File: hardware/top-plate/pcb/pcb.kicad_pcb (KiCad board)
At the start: 2 copper layers, 16 x 20 mm, 78 parts, among them SW1 MT-0-102-A101-M200-RS+PJ, U1 RP2040-ZERO

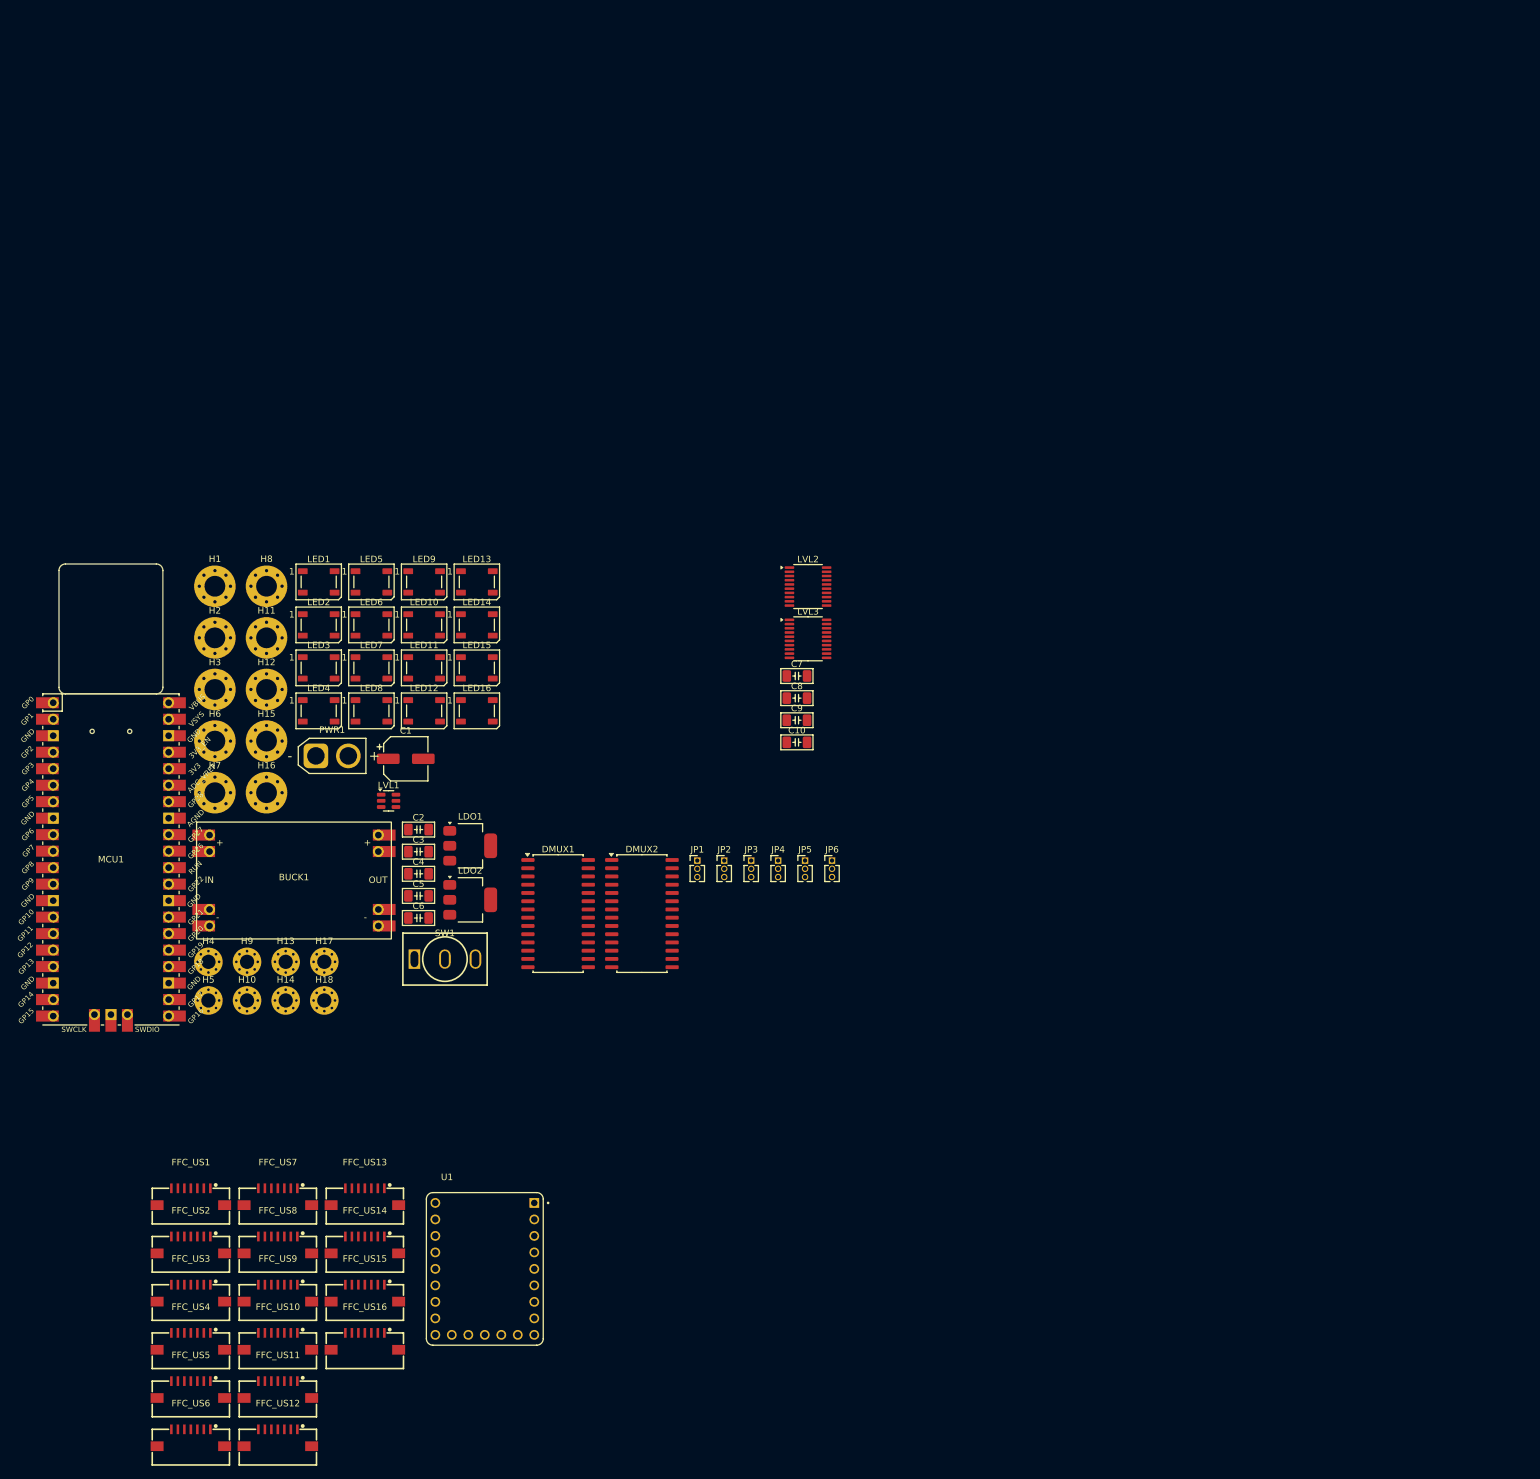
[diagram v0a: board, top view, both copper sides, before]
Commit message: some top plate changes
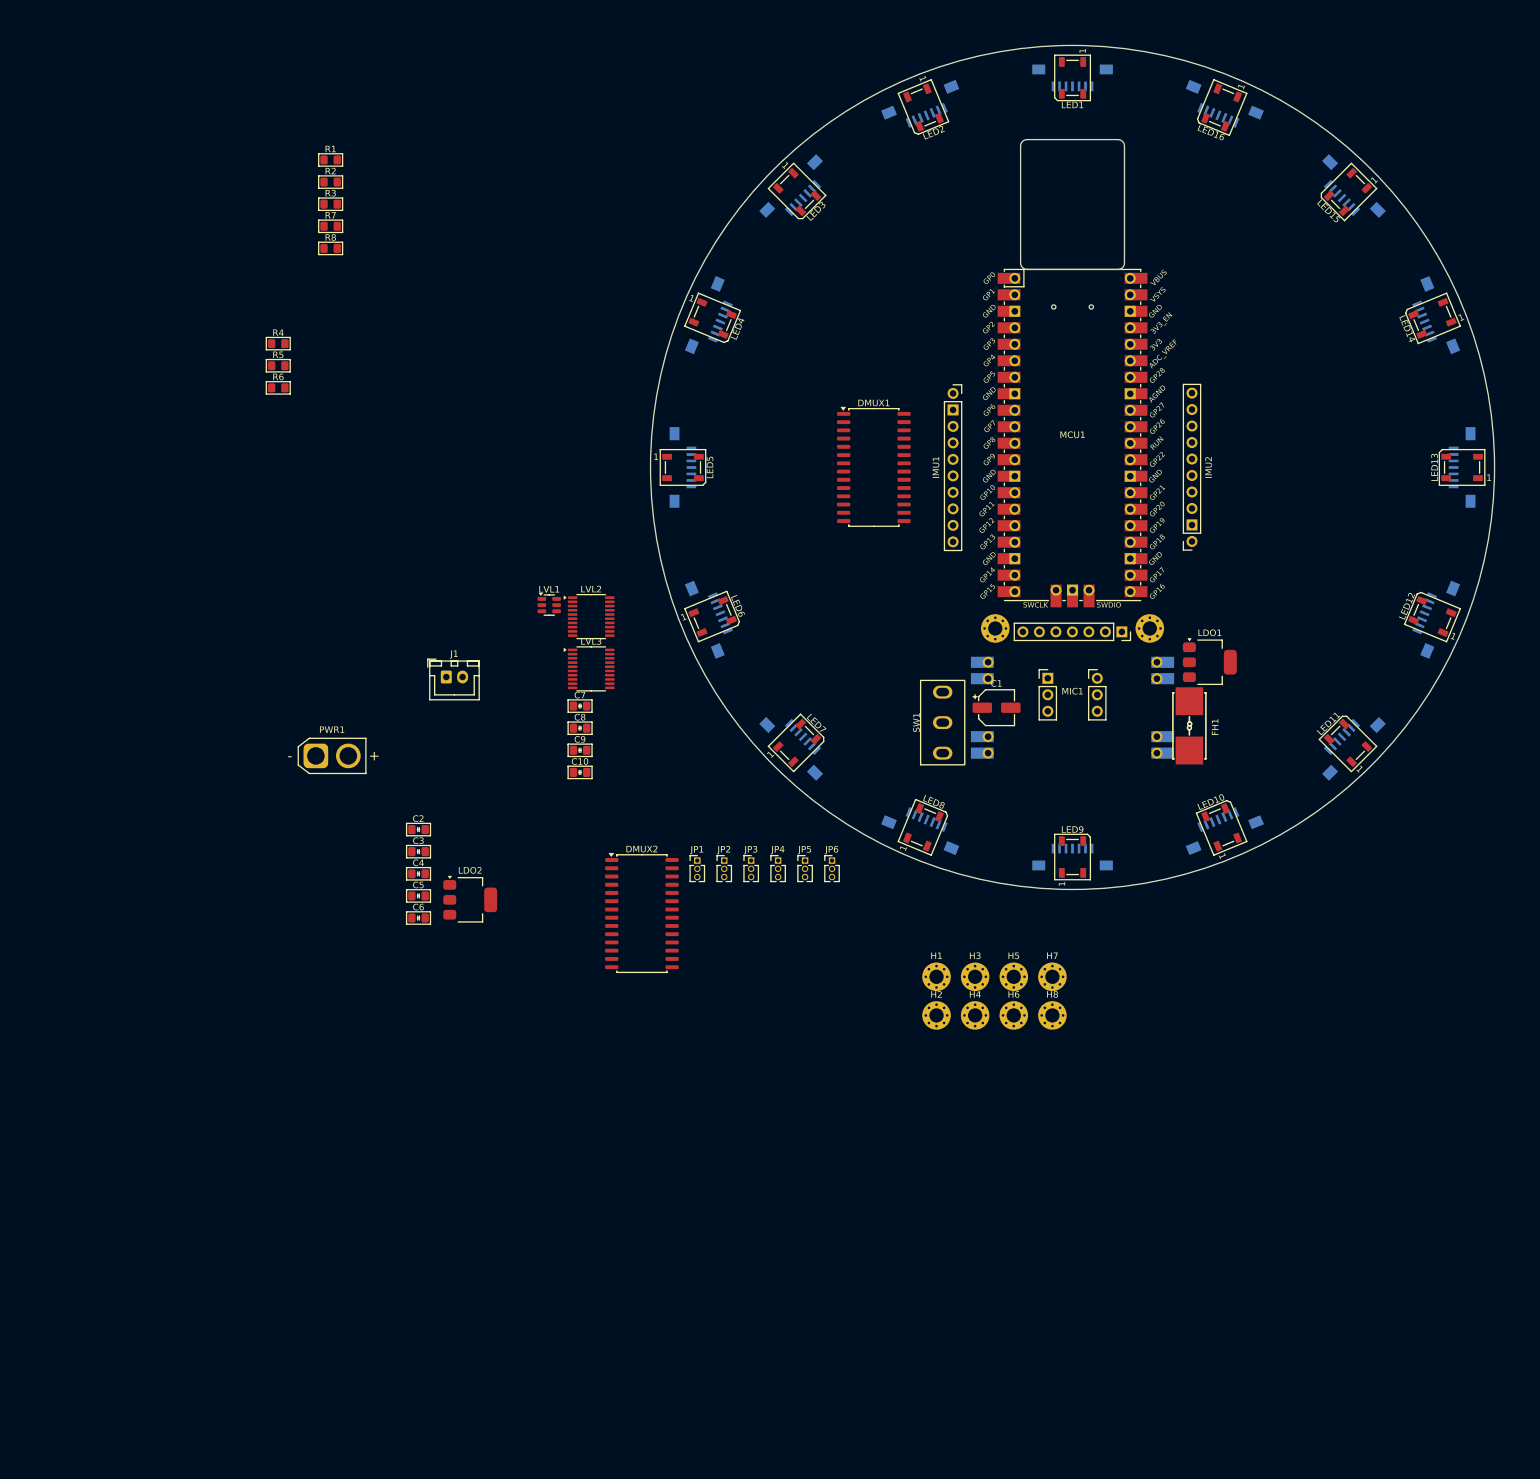
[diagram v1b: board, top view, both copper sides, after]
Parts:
- removed H10, H13, H14, H17, H18, H9: MountingHole_Pad, MountingHole:MountingHole_2.2mm_M2_Pad_Via
- removed H11, H12, H15, H16: MountingHole_Pad, MountingHole:MountingHole_3.2mm_M3_Pad_Via
- removed U1: RP2040-ZERO, Snapeda:RP2040-ZERO_MODULE_RP2040-ZERO
- added FH1: 01550900M, EasyEDA:FUSE-SMD_L9.8-W5.0, F.Cu at (18.0, 39.8)
- added IMU1: ~, ICM20948:ICM20948-no-mountingholes, F.Cu at (-12.0, 0.00)
- added IMU2: ~, ICM20948:ICM20948-no-mountingholes, F.Cu at (12.0, 0.00)
- added J1: Conn_01x02, Connector_JST:JST_XH_B2B-XH-A_1x02_P2.50mm_Vertical, F.Cu at (-96.5, 32.3)
- added MIC1: ~, INMP441:INMP441, F.Cu at (0.00, 35.0)
- added OLED1: ~, 0.96-inch_OLED_7-pin:0.96-inch_OLED_7-no-back-mountingholes, F.Cu at (0.00, 13.0)
- added R1: 2.2kR, PCM_Resistor_SMD_AKL:R_0805_2012Metric_Pad1.15x1.40mm_HandSolder, F.Cu at (-114.3, -47.4)
- added R2: 2.2kR, PCM_Resistor_SMD_AKL:R_0805_2012Metric_Pad1.15x1.40mm_HandSolder, F.Cu at (-114.3, -44.0)
- added R3: 10kR, PCM_Resistor_SMD_AKL:R_0805_2012Metric_Pad1.15x1.40mm_HandSolder, F.Cu at (-114.3, -40.5)
- added R4: 2.2kR, PCM_Resistor_SMD_AKL:R_0805_2012Metric_Pad1.15x1.40mm_HandSolder, F.Cu at (-122.3, -19.1)
- added R5: 2.2kR, PCM_Resistor_SMD_AKL:R_0805_2012Metric_Pad1.15x1.40mm_HandSolder, F.Cu at (-122.3, -15.7)
- added R6: 10kR, PCM_Resistor_SMD_AKL:R_0805_2012Metric_Pad1.15x1.40mm_HandSolder, F.Cu at (-122.3, -12.3)
- added R7: 10kR, PCM_Resistor_SMD_AKL:R_0805_2012Metric_Pad1.15x1.40mm_HandSolder, F.Cu at (-114.3, -37.1)
- added R8: 10kR, PCM_Resistor_SMD_AKL:R_0805_2012Metric_Pad1.15x1.40mm_HandSolder, F.Cu at (-114.3, -33.7)
- BUCK1, FFC_US1, FFC_US10, FFC_US11, FFC_US12, FFC_US13, FFC_US14, FFC_US15, FFC_US16, FFC_US2, FFC_US3, FFC_US4, FFC_US5, FFC_US6, FFC_US7, FFC_US8, FFC_US9: moved to B.Cu
- C1: footprint Capacitor_SMD:CP_Elec_6.3x7.7 -> Capacitor_SMD:CP_Elec_5x5.7
- C10, C2, C3, C4, C5, C6, C7, C8, C9: footprint PCM_Capacitor_SMD_AKL:C_1206_3216Metric_Pad1.33x1.80mm_HandSolder -> PCM_Capacitor_SMD_AKL:C_0805_2012Metric_Pad1.15x1.40mm_HandSolder
- H1, H2, H3, H6, H7, H8: footprint MountingHole:MountingHole_3.2mm_M3_Pad_Via -> MountingHole:MountingHole_2.2mm_M2_Pad_Via
- SW1: value MT-0-102-A101-M200-RS+PJ -> SS-12D10L5; footprint EasyEDA:SW-TH_MT-0-103-A101-M200-RS -> EasyEDA:SW-TH_SS-12D10L5
- moved FFC_US16 231.4 mm to (23.0, -55.4), turned to -22.5 degrees
- moved FFC_US15 227.4 mm to (42.4, -42.4), turned to -45 degrees
- moved FFC_US1 219.4 mm to (0.00, -60.0)
- moved FFC_US12 218.2 mm to (55.4, 23.0), turned to -112.5 degrees
- moved FFC_US14 217.7 mm to (55.4, -23.0), turned to -67.5 degrees
- moved FFC_US2 208.4 mm to (-23.0, -55.4), turned to 22.5 degrees
- moved FFC_US13 202.9 mm to (60.0, 0.00), turned to -90 degrees
- moved FFC_US3 193.6 mm to (-42.4, -42.4), turned to 45 degrees
- moved FFC_US11 192.6 mm to (42.4, 42.4), turned to -135 degrees
- moved FFC_US4 176.9 mm to (-55.4, -23.0), turned to 67.5 degrees
- moved FFC_US10 165.5 mm to (23.0, 55.4), turned to -157.5 degrees
- moved MCU1 161.9 mm to (0.00, -5.00)
- moved FFC_US5 161.0 mm to (-60.0, 0.00), turned to 90 degrees
- moved LED12 156.0 mm to (55.4, 23.0), turned to 157.5 degrees
- moved LED14 154.6 mm to (55.4, -23.0), turned to -157.5 degrees
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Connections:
- BUCK1 pad 3: +5V -> Net-(BUCK1-OUT+)
- C2 pad 2: +5V -> Net-(BUCK1-OUT+)
- LVL2 pad 10: +1V8 -> Net-(LVL2-OE)
- LVL3 pad 10: +1V8 -> Net-(LVL3-OE)
- LVL3 pad 16: /PROGMUX_INTB -> /CH201/PROGMUX_INTB
- LVL3 pad 18: /INTMUX_INTB -> /CH201/INTMUX_INTB
- MCU1 pad 10: /INTMUX_INTB -> /IMU1.NCS
- MCU1 pad 11: /PROGMUX_INTA -> /IMU2.INT
- MCU1 pad 12: /PROGMUX_INTB -> /IMU2.NCS
- MCU1 pad 16: /SPI1.MISO -> /US_NRST
- MCU1 pad 17: /SCREEN_SCS -> /PROGMUX_INTA
- MCU1 pad 24: /US_NRST -> /MIC1.SCK
- MCU1 pad 25: unconnected-(MCU1-GPIO19-Pad25) -> /MIC1.WS
- MCU1 pad 26: unconnected-(MCU1-GPIO20-Pad26) -> /MIC1.L/R
- MCU1 pad 27: unconnected-(MCU1-GPIO21-Pad27) -> /MIC1.SD
- MCU1 pad 29: unconnected-(MCU1-GPIO22-Pad29) -> /OLED.SCS
- MCU1 pad 31: unconnected-(MCU1-GPIO26_ADC0-Pad31) -> /OLED.D/C#
- MCU1 pad 32: unconnected-(MCU1-GPIO27_ADC1-Pad32) -> /OLED.NRST
- MCU1 pad 34: unconnected-(MCU1-GPIO28_ADC2-Pad34) -> /INTMUX_INTA
- MCU1 pad 9: /INTMUX_INTA -> /IMU1.INT
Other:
- board size 16 x 20 mm -> 130 x 130 mm

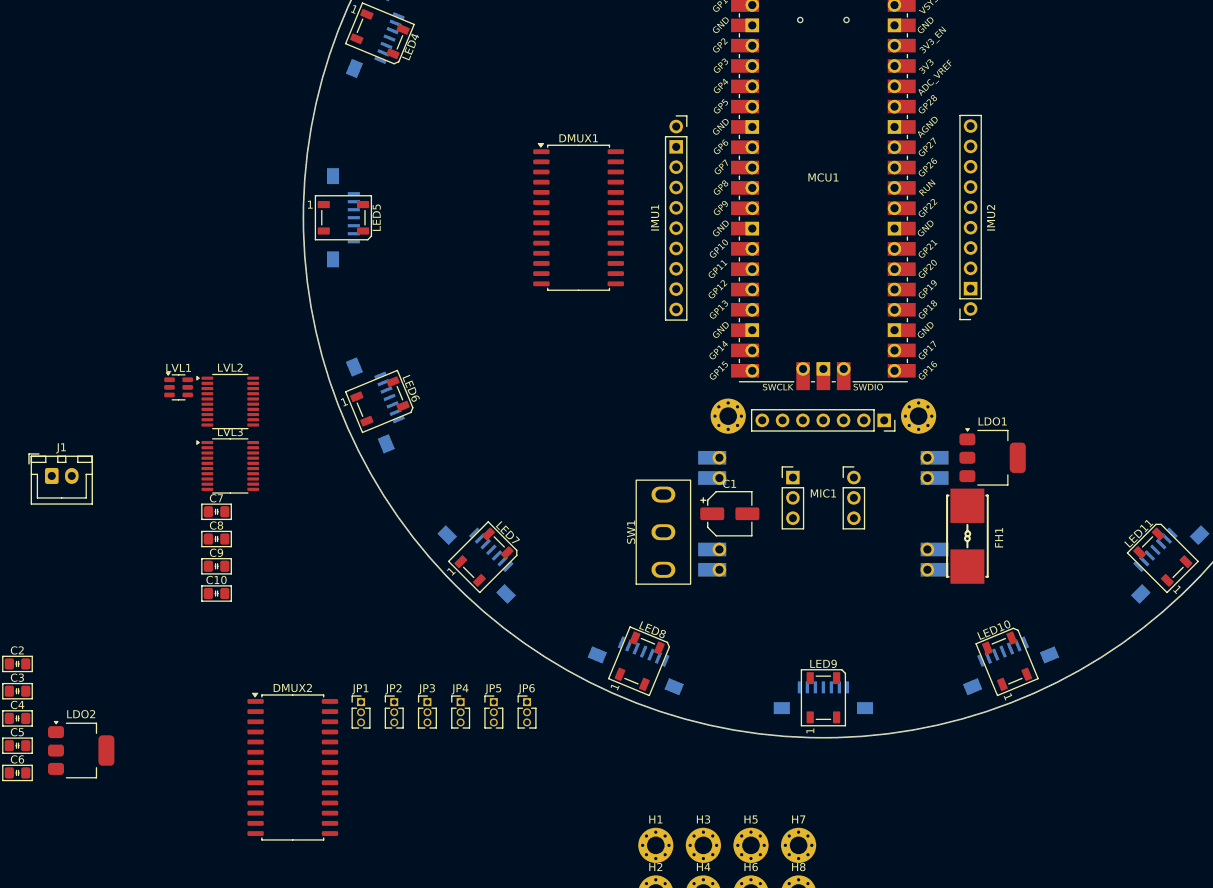
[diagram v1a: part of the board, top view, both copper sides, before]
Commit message: fixed up bottom plate schematic. do not run a global symbol update! all modified symbols as of now are intentionally modified locally.
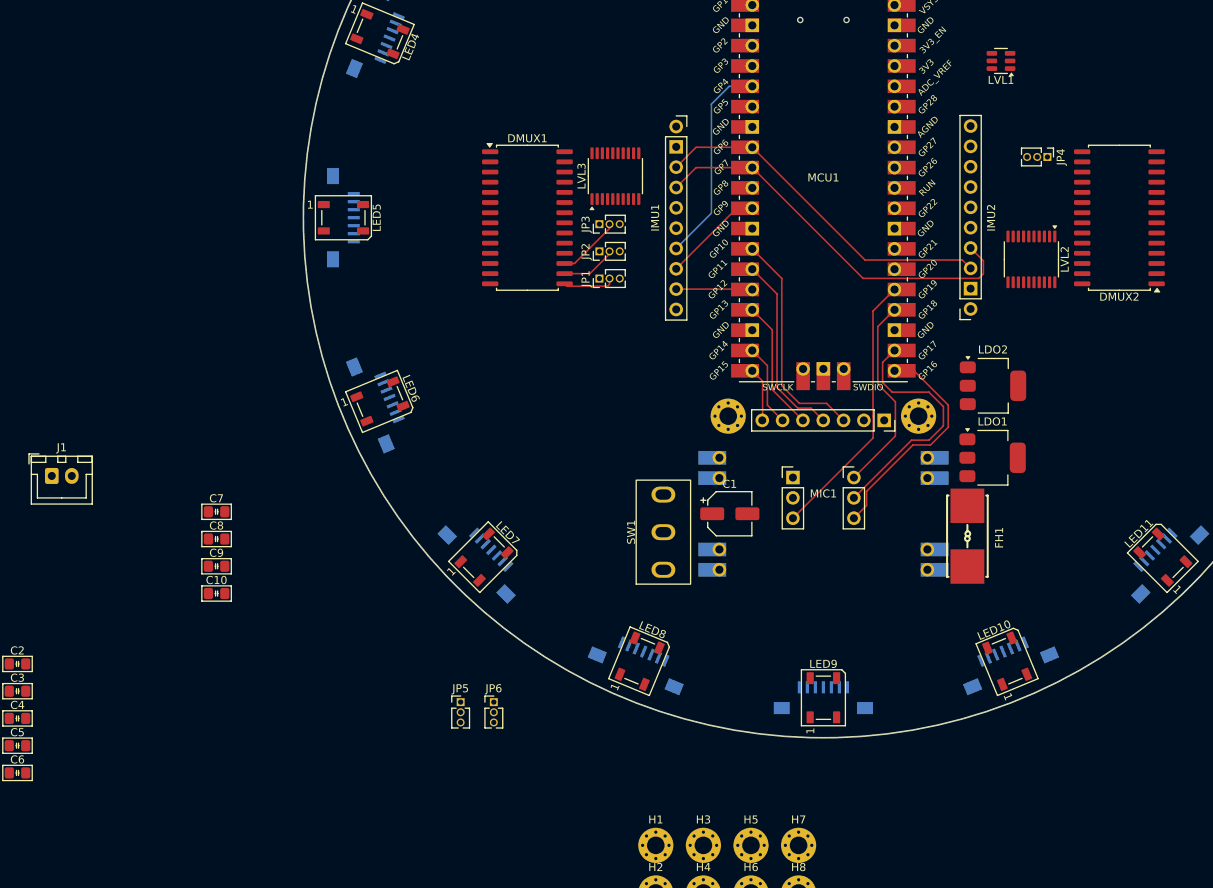
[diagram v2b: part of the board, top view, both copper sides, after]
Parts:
- moved DMUX2 124.1 mm to (37.0, 0.00), turned to 180 degrees
- moved LDO2 122.8 mm to (21.2, 21.0)
- moved LVL1 110.6 mm to (22.2, -19.6), turned to 180 degrees
- moved LVL2 101.7 mm to (26.0, 5.20), turned to -90 degrees
- moved JP4 94.2 mm to (28.0, -7.60), turned to -90 degrees
- moved JP3 65.0 mm to (-28.0, 0.80), turned to 90 degrees
- moved JP2 63.7 mm to (-28.0, 4.20), turned to 90 degrees
- moved LVL3 60.2 mm to (-26.0, -5.20), turned to 90 degrees
- moved JP1 57.1 mm to (-28.0, 7.60), turned to 90 degrees
- moved DMUX1 6.40 mm to (-37.0, 0.00)
- renumbered JP3 to JP1, JP1 to JP2, JP2 to JP3, JP6 to JP4, JP4 to JP5, JP5 to JP6
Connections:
- net /CH201/INTMUX_INTA_1V8 renamed /CH201/DMUX1_INTA_1V8
- net /CH201/INTMUX_INTB renamed /CH201/DMUX1_INTB
- net /CH201/INTMUX_INTB_1V8 renamed /CH201/DMUX1_INTB_1V8
- net /CH201/PROGMUX_INTA_1V8 renamed /CH201/DMUX2_INTA_1V8
- net /CH201/PROGMUX_INTB renamed /CH201/DMUX2_INTB
- net /CH201/PROGMUX_INTB_1V8 renamed /CH201/DMUX2_INTB_1V8
- net /INTMUX_INTA renamed /DMUX1_INTA
- DMUX1 pad 2: /CH201/US_INT2 -> /CH201/US_PROG1
- DMUX1 pad 21: /CH201/US_INT9 -> /CH201/US_INT5
- DMUX1 pad 22: /CH201/US_INT10 -> /CH201/US_PROG5
- DMUX1 pad 23: /CH201/US_INT11 -> /CH201/US_INT6
- DMUX1 pad 24: /CH201/US_INT12 -> /CH201/US_PROG6
- DMUX1 pad 25: /CH201/US_INT13 -> /CH201/US_INT7
- DMUX1 pad 26: /CH201/US_INT14 -> /CH201/US_PROG7
- DMUX1 pad 27: /CH201/US_INT15 -> /CH201/US_INT8
- DMUX1 pad 28: /CH201/US_INT16 -> /CH201/US_PROG8
- DMUX1 pad 3: /CH201/US_INT3 -> /CH201/US_INT2
- DMUX1 pad 4: /CH201/US_INT4 -> /CH201/US_PROG2
- DMUX1 pad 5: /CH201/US_INT5 -> /CH201/US_INT3
- DMUX1 pad 6: /CH201/US_INT6 -> /CH201/US_PROG3
- DMUX1 pad 7: /CH201/US_INT7 -> /CH201/US_INT4
- DMUX1 pad 8: /CH201/US_INT8 -> /CH201/US_PROG4
- DMUX2 pad 1: /CH201/US_PROG1 -> /CH201/US_INT9
- DMUX2 pad 2: /CH201/US_PROG2 -> /CH201/US_PROG9
- DMUX2 pad 21: /CH201/US_PROG9 -> /CH201/US_INT13
- DMUX2 pad 22: /CH201/US_PROG10 -> /CH201/US_PROG13
- DMUX2 pad 23: /CH201/US_PROG11 -> /CH201/US_INT14
- DMUX2 pad 24: /CH201/US_PROG12 -> /CH201/US_PROG14
- DMUX2 pad 25: /CH201/US_PROG13 -> /CH201/US_INT15
- DMUX2 pad 26: /CH201/US_PROG14 -> /CH201/US_PROG15
- DMUX2 pad 27: /CH201/US_PROG15 -> /CH201/US_INT16
- DMUX2 pad 3: /CH201/US_PROG3 -> /CH201/US_INT10
- DMUX2 pad 4: /CH201/US_PROG4 -> /CH201/US_PROG10
- DMUX2 pad 5: /CH201/US_PROG5 -> /CH201/US_INT11
- DMUX2 pad 6: /CH201/US_PROG6 -> /CH201/US_PROG11
- DMUX2 pad 7: /CH201/US_PROG7 -> /CH201/US_INT12
- DMUX2 pad 8: /CH201/US_PROG8 -> /CH201/US_PROG12
- LVL3 pad 17: /PROGMUX_INTA -> /DMUX2_INTA
- MCU1 pad 10: /IMU1.NCS -> /SPI0.MOSI
- MCU1 pad 11: /IMU2.INT -> unconnected-(MCU1-GPIO8-Pad11)
- MCU1 pad 12: /IMU2.NCS -> /IMU1.INT
- MCU1 pad 16: /US_NRST -> /IMU1.NCS
- MCU1 pad 17: /PROGMUX_INTA -> /OLED.NRST
- MCU1 pad 19: /I2C1.SDA -> /OLED.D/C#
- MCU1 pad 20: /I2C1.SCL -> /OLED.SCS
- MCU1 pad 21: /LED_SIG_DIR -> /MIC1.SCK
- MCU1 pad 22: /LED_SIG_3V3 -> /MIC1.WS
- MCU1 pad 24: /MIC1.SCK -> /MIC1.L/R
- MCU1 pad 25: /MIC1.WS -> /MIC1.SD
- MCU1 pad 26: /MIC1.L/R -> unconnected-(MCU1-GPIO20-Pad26)
- MCU1 pad 27: /MIC1.SD -> unconnected-(MCU1-GPIO21-Pad27)
- MCU1 pad 29: /OLED.SCS -> unconnected-(MCU1-GPIO22-Pad29)
- MCU1 pad 31: /OLED.D/C# -> unconnected-(MCU1-GPIO26_ADC0-Pad31)
- MCU1 pad 32: /OLED.NRST -> unconnected-(MCU1-GPIO27_ADC1-Pad32)
- MCU1 pad 4: /SPI0.SCLK -> unconnected-(MCU1-GPIO2-Pad4)
- MCU1 pad 5: /SPI0.MOSI -> unconnected-(MCU1-GPIO3-Pad5)
- MCU1 pad 9: /IMU1.INT -> /SPI0.SCLK
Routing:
- net /SPI0.MOSI: track 0.00 -> 49.3 mm
- net /SPI0.SCLK: track 0.00 -> 44.1 mm
- net /MIC1.SD: track 0.00 -> 33.9 mm
- net /MIC1.WS: track 0.00 -> 30.8 mm
- net /MIC1.SCK: track 0.00 -> 28.8 mm
- net /SPI1.SCLK: track 0.00 -> 28.1 mm
- net /SPI0.MISO: track 0.00 -> 25.9 mm
- net /MIC1.L/R: track 0.00 -> 24.9 mm
- net /SPI1.MOSI: track 0.00 -> 23.5 mm
- net /OLED.NRST: track 0.00 -> 16.4 mm
- net /IMU1.INT: track 0.00 -> 12.6 mm
- net /OLED.D/C#: track 0.00 -> 10.3 mm
- net /IMU1.NCS: track 0.00 -> 9.53 mm
- net Net-(DMUX1-A2): track 0.00 -> 7.97 mm
- net Net-(DMUX1-A1): track 0.00 -> 6.97 mm
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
